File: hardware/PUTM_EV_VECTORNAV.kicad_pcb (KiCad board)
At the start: 4 copper layers, 70 x 70 mm, 91 parts, among them J1 Conn_01x02, J2 uFL ant, J3 SMA ant, J4 uFL ant, J5 SMA ant, J6 Conn_01x02, J7 USB_A, J8 FTSH-107-01-L-D-K, J9 XIAO ESP32S3 Sense, Q1 NMOS, Q2 SI2347DS-T1-GE3, U1 VN-300, U2 STM32G0C1KCTxN, U3 ADM3057ExRW, U4 FT231XS-U, U5 API7721FSB-13, U6 AQY284S, U7 NCP565D2T33R4G, U8 SI06W8-05

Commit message: Finished pcb routing
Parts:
- moved C21 3.00 mm to (143.8, 110.5)
- moved C10 1.90 mm to (167.2, 86.0)
- moved R9 1.35 mm to (167.3, 84.2)
- moved D14 0.75 mm to (143.5, 102.8)
- moved R16 0.75 mm to (140.0, 102.8)
- moved D7 0.40 mm to (120.2, 105.8)
- moved R12 0.20 mm to (130.5, 61.8)
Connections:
- C18 pad 1: Net-(U8--VIN) -> Net-(U8-+VIN)
- C19 pad 1: Net-(U8--VIN) -> Net-(U8-+VIN)
- D6 pad 1: /CAN/CAN+ -> /CAN/CAN-
- D6 pad 2: /CAN/CAN- -> /CAN/CAN+
- L1 pad 2: Net-(U8--VIN) -> Net-(U8-+VIN)
- U8 pad 1: GND_EXT -> Net-(U8-+VIN)
- U8 pad 2: Net-(U8--VIN) -> GND_EXT
- U8 pad 4: +5V -> GND
- U8 pad 6: GND -> +5V
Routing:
- net +3.3V: track 9.92 -> 191.5 mm, vias 0 -> 5
- net +5V: track 0.00 -> 140.4 mm
- net GND: track 0.00 -> 53.6 mm, vias 0 -> 35
- net 3V3_USB: track 13.8 -> 57.2 mm, vias 0 -> 4
- net /CAN/CAN-: track 0.00 -> 26.2 mm, vias 0 -> 2
- net /CAN/CAN+: track 0.00 -> 26.1 mm, vias 0 -> 2
- net Net-(BT1-+): track 0.00 -> 23.1 mm
- net Net-(U8-+VIN): track 0.00 -> 20.3 mm
- net /CAN/GND_CAN_ISO: track 0.00 -> 16.2 mm, vias 0 -> 6
- net Net-(D13-K): track 0.00 -> 15.6 mm
- net Net-(D12-A2): track 0.00 -> 15.4 mm
- net Net-(U3-VISOIN): track 0.00 -> 14.6 mm
- net /Connectors/PROG_RX: track 12.8 -> 26.9 mm, vias 1 -> 2
- net /Connectors/PROG_TX: track 16.1 -> 28.0 mm, vias 1 -> 2
- net Net-(C8-Pad1): track 0.00 -> 11.7 mm, vias 0 -> 2
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- added copper zone on In1.Cu, net /CAN/GND_CAN_ISO
- added copper zone on In2.Cu, net /CAN/GND_CAN_ISO
- added copper zone on In1.Cu, net GND
- added copper zone on In2.Cu, net GND
- added copper zone on In1.Cu, net GND_EXT
- added copper zone on In2.Cu, net GND_EXT
- added copper zone on In1.Cu, net GND_USB
- added copper zone on In2.Cu, net GND_USB
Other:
- board text added: "C4"

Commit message: Finished routing
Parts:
- removed REF** (x4): MountingHole_3mm_Pad_Via, MountingHole:MountingHole_3mm_Pad_Via
- added H1: MountingHole_Pad, MountingHole:MountingHole_3mm_Pad_Via, F.Cu at (105.0, 35.0)
- added H2: MountingHole_Pad, MountingHole:MountingHole_3mm_Pad_Via, F.Cu at (185.0, 35.0)
- added H3: MountingHole_Pad, MountingHole:MountingHole_3mm_Pad_Via, F.Cu at (185.0, 95.0)
- added H4: MountingHole_Pad, MountingHole:MountingHole_3mm_Pad_Via, F.Cu at (105.0, 95.0)
- added TP1: 24V_TestPoint, TestPoint:TestPoint_Pad_D1.0mm, F.Cu at (111.2, 65.5)
- added TP2: 5V_TestPoint, TestPoint:TestPoint_Pad_D1.0mm, F.Cu at (120.5, 65.5)
- added TP3: 3V3_TestPoint, TestPoint:TestPoint_Pad_D1.0mm, F.Cu at (114.0, 97.8)
- added TP4: RSTR, TestPoint:TestPoint_Pad_D1.0mm, F.Cu at (148.0, 63.5)
- added TP5: NRST, TestPoint:TestPoint_Pad_D1.0mm, F.Cu at (148.0, 61.5)
- added TP6: EN, TestPoint:TestPoint_Pad_D1.0mm, F.Cu at (148.2, 55.0)
- added TP7: CS, TestPoint:TestPoint_Pad_D1.0mm, F.Cu at (148.0, 69.0)
- added TP8: BAT, TestPoint:TestPoint_Pad_D1.0mm, F.Cu at (161.2, 44.8)
- C17: value 2.2uF -> 10uF; footprint Capacitor_SMD:C_1206_3216Metric_Pad1.33x1.80mm_HandSolder -> 10uF24Vcap:CAPC6050X550N
- C21: value 47uF+ -> 20uF; footprint 47uCapPolarized:EEE1AA220WR -> 20uF5Vcap:GRM31x
- L1: value 10uH -> 3.9uH; footprint inductor:VLS3010 -> inductor:RLS397
- U8: value SI06W8-05 -> RSH3-2405S_H2; footprint DCisoconv:SI06W805 -> DCisoconv:RSH32405SH2
- moved Q2 86.7 mm to (102.5, 72.8), turned to 90 degrees
- moved R15 84.9 mm to (102.5, 76.0), turned to 180 degrees
- moved J6 84.2 mm to (102.0, 62.1), turned to 90 degrees
- moved D12 83.7 mm to (102.5, 67.5), turned to -90 degrees
- moved J1 83.5 mm to (102.0, 54.5), turned to 90 degrees
- moved D13 81.6 mm to (102.2, 79.3), turned to 90 degrees
- moved F1 81.3 mm to (105.2, 68.0)
- moved D6 79.4 mm to (103.8, 40.0)
- moved L1 76.5 mm to (107.5, 74.0), turned to 90 degrees
- moved C19 76.1 mm to (115.8, 65.5), turned to 0 degrees
- moved C18 75.4 mm to (108.5, 68.8), turned to 90 degrees
- moved R9 75.0 mm to (109.5, 36.5), turned to 90 degrees
- moved C7 73.5 mm to (103.0, 45.8), turned to -90 degrees
- moved C10 72.8 mm to (109.2, 42.0), turned to 90 degrees
- moved C9 72.1 mm to (107.8, 42.0), turned to -90 degrees
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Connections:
- D11 pad 3: /Connectors/PROG_SWCLK -> /Connectors/PROG_SWDIO
- D11 pad 4: /Connectors/PROG_SWDIO -> /Connectors/PROG_SWCLK
- D3 pad 1: /Connectors/d+ -> /Connectors/D+
- D3 pad 2: /Connectors/d- -> /Connectors/D-
- D6 pad 1: /CAN/CAN- -> /CAN/CAN+
- D6 pad 2: /CAN/CAN+ -> /CAN/CAN-
- U8 pad 1: Net-(U8-+VIN) -> GND_EXT
- U8 pad 2: GND_EXT -> unconnected-(U8-CTRL-Pad2)
- U8 pad 6: +5V -> unconnected-(U8-NC_1-Pad6)
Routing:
- net +5V: track 140.4 -> 103.1 mm, vias 0 -> 2
- net /MCU/VN_CS: track 3.25 -> 37.0 mm
- net Net-(U1-ENABLE): track 45.3 -> 14.1 mm
- net /VectorNav/GPS_PPS: track 5.10 -> 36.1 mm
- net Net-(U1-NRST): track 4.26 -> 33.3 mm
- net /MCU/VN_RESTORE: track 36.9 -> 8.87 mm, vias 2 -> 0
- net +3.3V: track 191.5 -> 167.5 mm
- net Net-(U1-SPI_MISO): track 5.37 -> 27.9 mm
- net /Connectors/XIAO_GPIO: track 17.1 -> 35.6 mm
- net /Connectors/XIAO_TX: track 11.6 -> 27.1 mm
- net Net-(U1-RESTORE): track 7.99 -> 22.9 mm, vias 0 -> 2
- net /Connectors/XIAO_RX: track 24.4 -> 9.67 mm
- net /MCU/VN_GNSS_SYNC: track 26.7 -> 41.3 mm, vias 2 -> 0
- net 3V3_USB: track 57.2 -> 43.0 mm
- net /MCU/vnCS: track 1.98 -> 14.2 mm
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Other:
- board size 70 x 70 mm -> 90 x 70 mm
- board text added: "24V"
- board text added: "3V3"
- board text added: "5V"
- board text added: "CS"
- board text added: "EN"
- board text added: "NRST"
- board text added: "RSTR"
- board text removed: "C4"

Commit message: Some smaller fixes and final aesthetic changes
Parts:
- removed C17: 10uF, 10uF24Vcap:CAPC6050X550N
- removed C18: 2.2uF, Capacitor_SMD:C_1206_3216Metric_Pad1.33x1.80mm_HandSolder
- added C26: 1uF, Capacitor_SMD:C_0603_1608Metric_Pad1.08x0.95mm_HandSolder, F.Cu at (160.2, 59.0)
- added C27: 10uF, Capacitor_SMD:C_1206_3216Metric, F.Cu at (107.8, 78.5)
- added C28: 10uF, Capacitor_SMD:C_1206_3216Metric, F.Cu at (107.8, 81.0)
- added C29: 10uF, Capacitor_SMD:C_1206_3216Metric, F.Cu at (107.8, 83.5)
- added C30: 10uF, Capacitor_SMD:C_1206_3216Metric, F.Cu at (107.8, 70.2)
- added C31: 10uF, Capacitor_SMD:C_1206_3216Metric, F.Cu at (107.8, 67.8)
- added C32: 10uF, Capacitor_SMD:C_1206_3216Metric, F.Cu at (107.8, 65.2)
- added REF**: ICHTIS, PUTM_logo:PUTM_logo, F.Cu at (175.0, 65.0)
- added REF**: PUTM_logo, PUTM_logo:PUTM_logo, B.Cu at (181.0, 57.5)
- added TP10: VN_RX, TestPoint:TestPoint_Pad_D1.0mm, F.Cu at (158.8, 67.5)
- added TP11: D-, TestPoint07:TestPoint_Pad_D0.7mm, F.Cu at (148.7, 87.4)
- added TP12: D+, TestPoint07:TestPoint_Pad_D0.7mm, F.Cu at (146.8, 87.4)
- added TP9: VN_TX, TestPoint:TestPoint_Pad_D1.0mm, F.Cu at (158.8, 65.0)
- H1, H2, H3: footprint MountingHole:MountingHole_3mm_Pad_Via -> MountingHole:MountingHole_3mm
- moved F1 3.40 mm to (102.5, 66.0)
- moved D12 3.25 mm to (102.5, 70.8), turned to 90 degrees
- moved D13 3.25 mm to (102.2, 82.6)
- moved Q2 3.25 mm to (102.5, 76.0)
- moved R15 3.01 mm to (102.2, 79.0), turned to 0 degrees
- moved C12 0.75 mm to (152.8, 90.2)
- moved D2 0.75 mm to (153.2, 88.2)
- moved D3 0.75 mm to (147.7, 89.8)
- moved J7 0.75 mm to (151.2, 97.0)
- moved C21 0.50 mm to (126.5, 65.5), turned to 180 degrees
- moved L1 0.35 mm to (107.8, 74.2)
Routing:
- net Net-(D16-A2): track 27.5 -> 1.34 mm
- net Net-(D15-A2): track 25.0 -> 0.00 mm
- net Net-(U8-+VIN): track 14.2 -> 19.5 mm
- net Net-(D12-A2): track 5.46 -> 10.5 mm
- net Net-(D13-K): track 14.7 -> 18.0 mm
- net +24V_EXT: track 11.3 -> 8.82 mm
- net GND: track 62.7 -> 60.4 mm, vias 117 -> 60
- net +3.3V: track 167.5 -> 166.3 mm
- net Net-(D13-A): track 4.06 -> 5.01 mm
- net Net-(U1-VBAT): track 36.8 -> 37.6 mm
- net Net-(D2-A1): track 10.6 -> 11.4 mm
- net /Connectors/D-: track 10.6 -> 11.3 mm
- net /Connectors/D+: track 10.5 -> 11.3 mm
- net GND_EXT: track 16.1 -> 15.8 mm, vias 8 -> 16
- added copper zone on F.Cu, net GND
- added copper zone on F.Cu, net GND_EXT
- added copper zone on F.Cu, net Net-(D15-A2)
- added copper zone on In1.Cu, net Net-(D15-A2)
- added copper zone on F.Cu, net Net-(D16-A2)
- added copper zone on In1.Cu, net Net-(D16-A2)
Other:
- board text added: "BAT"
- board text added: "D+"
- board text added: "D-"
- board text added: "VN_RX"
- board text added: "VN_TX"

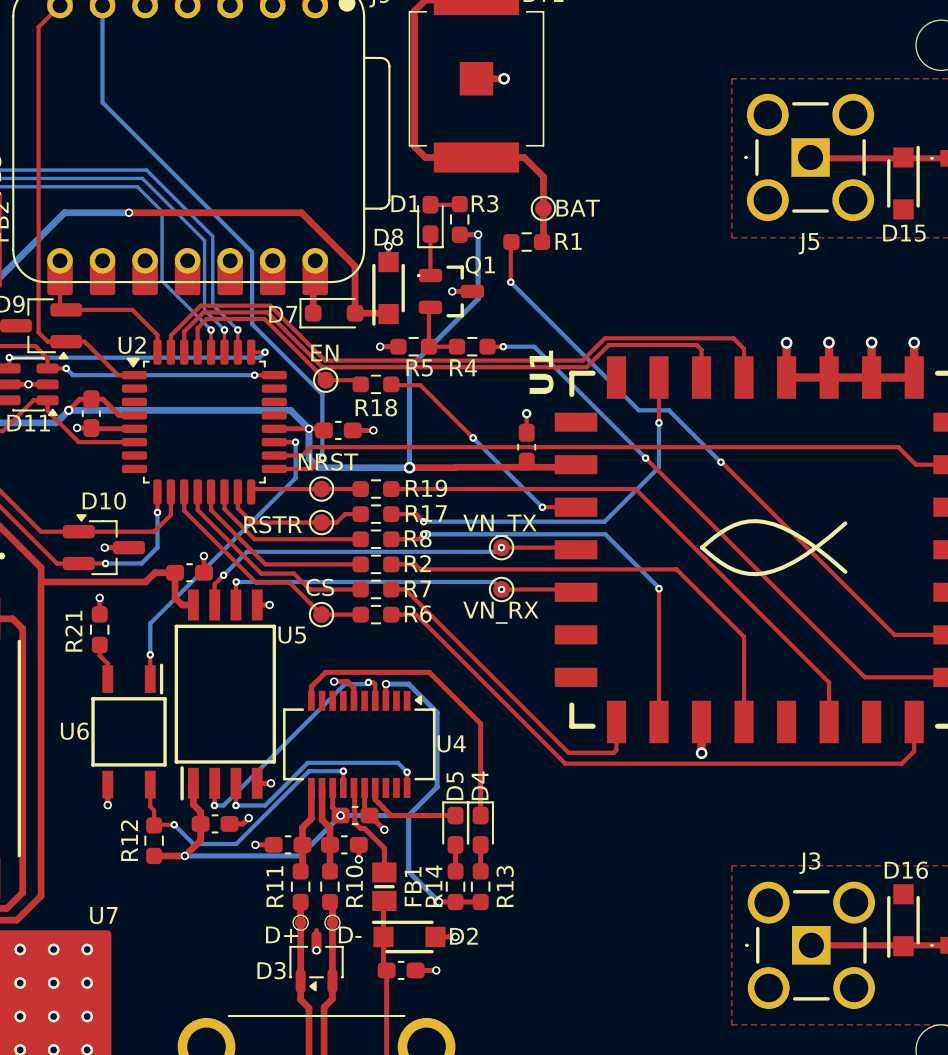
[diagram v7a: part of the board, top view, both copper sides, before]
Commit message: little changes with traces and 3D models visibility
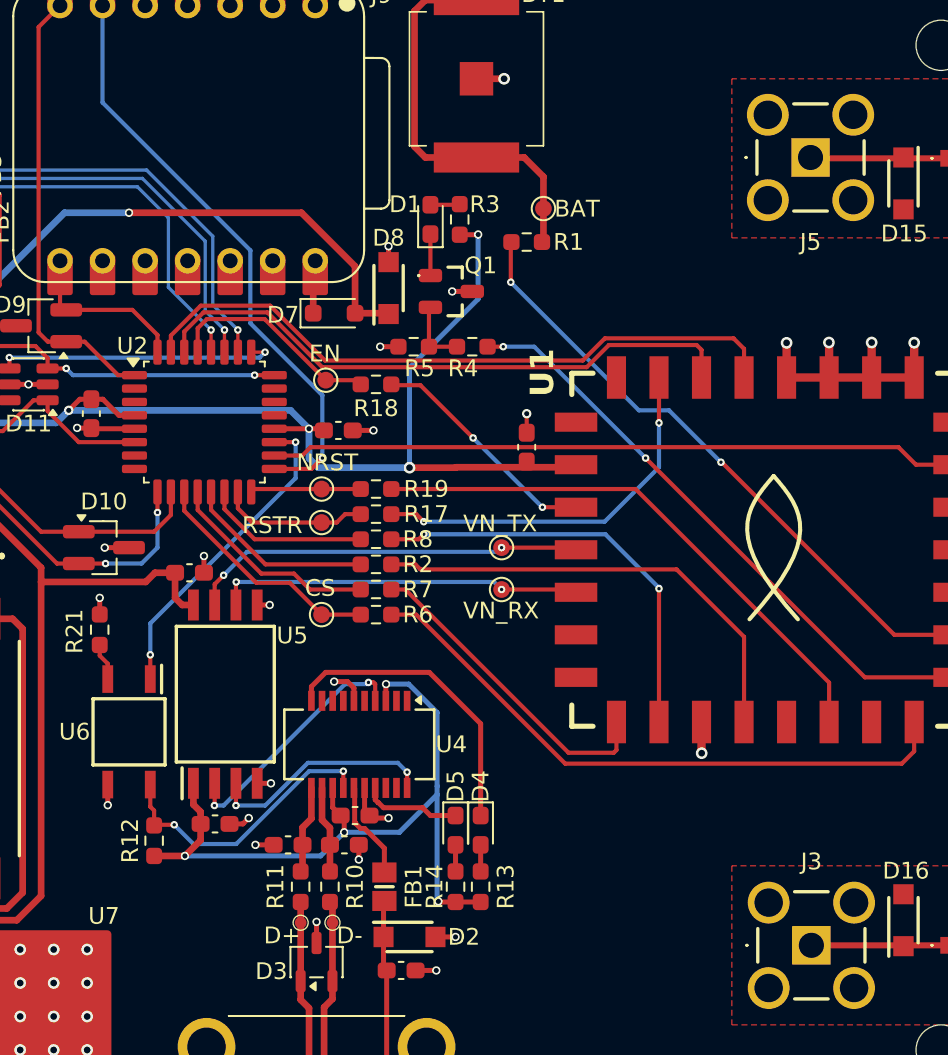
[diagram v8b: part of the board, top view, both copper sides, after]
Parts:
- turned REF** to -90 degrees
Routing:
- net 3V3_USB: track 43.0 -> 44.9 mm
